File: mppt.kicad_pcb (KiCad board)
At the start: 2 copper layers, 52 parts, among them P101 CONN_01X02, P102 CONN_01X02, P103 JTAG, P104 CONN_01X02, Q201 IRF7343PBF, U102 STM32F103C8Tx, U104 SN65HVD12DR, U201 358, U202 358, U301 lm2575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

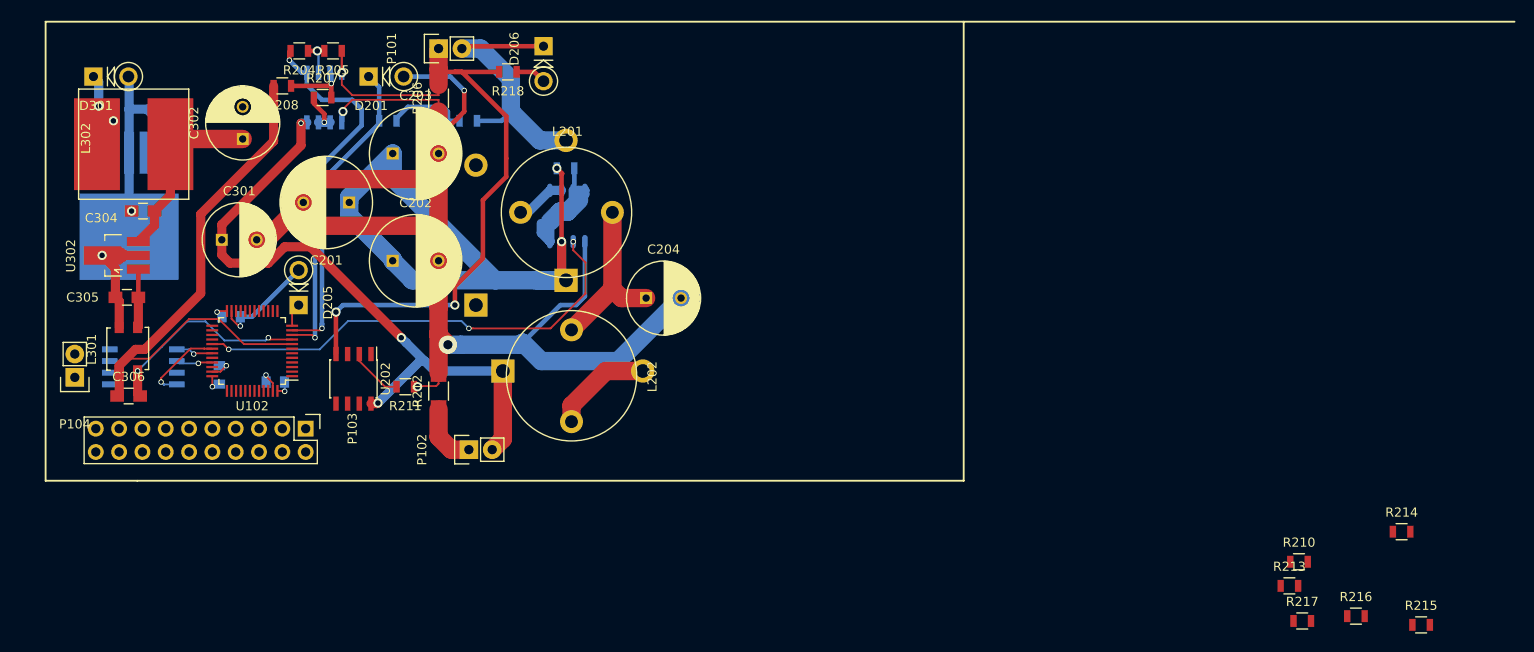
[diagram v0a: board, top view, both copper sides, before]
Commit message: Changed a bit, and did a full re-route
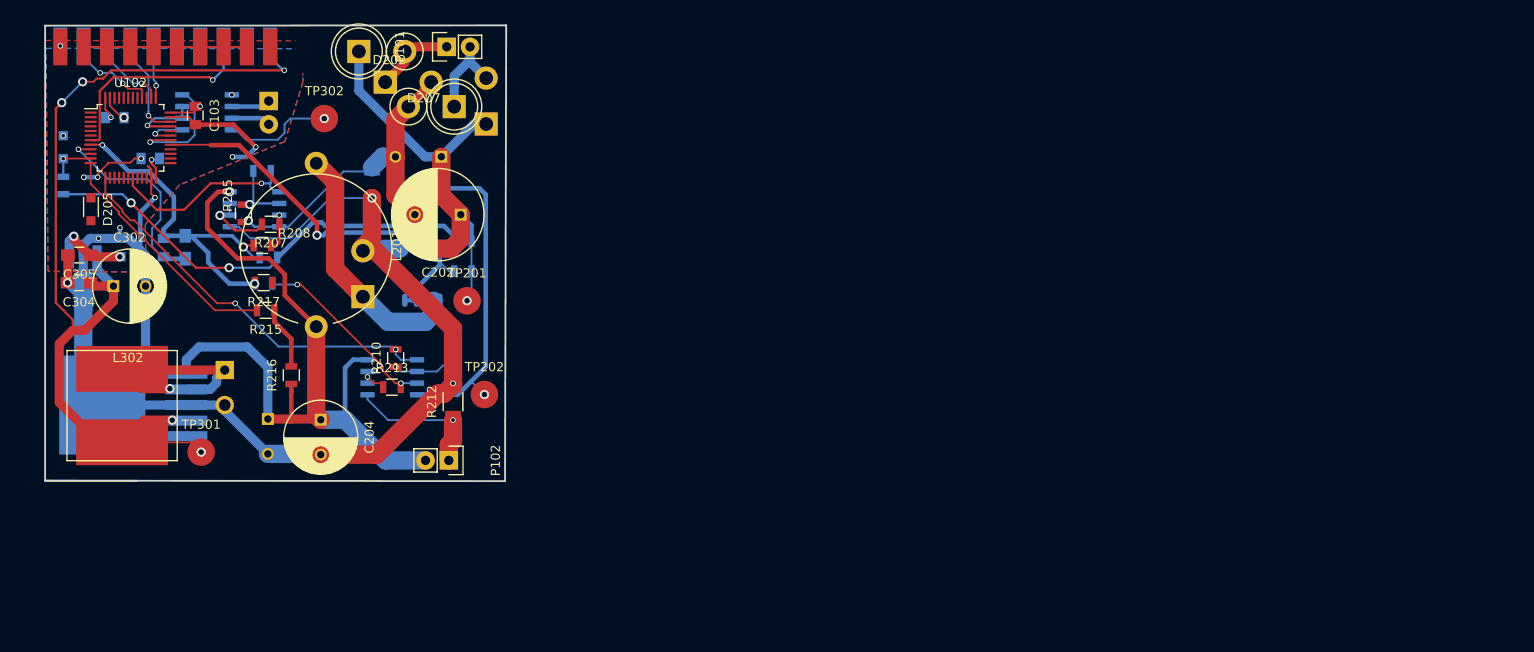
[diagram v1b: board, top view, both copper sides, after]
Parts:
- removed C203: CP, Capacitors_ThroughHole:C_Radial_D10_L16_P5
- removed L202: L, Inductors_NEOSID:Neosid_Inductor_Sd14
- removed R218: R, Resistors_SMD:R_0805
- removed U104: SN65HVD12DR, Housings_SOIC:SOIJ-8_5.3x5.3mm_Pitch1.27mm
- added D207: D_Schottky, lib:Diode_DO-201AD_Vertical, F.Cu at (74.1, 43.2)
- added TP201: TEST, Measurement_Points:Measurement_Point_Round-SMD-Pad_Big, F.Cu at (85.9, 70.4)
- added TP202: TEST, Measurement_Points:Measurement_Point_Round-SMD-Pad_Big, F.Cu at (87.8, 80.6)
- added TP301: TEST, Measurement_Points:Measurement_Point_Round-SMD-Pad_Big, F.Cu at (56.9, 86.9)
- added TP302: TEST, Measurement_Points:Measurement_Point_Round-SMD-Pad_Big, F.Cu at (70.4, 50.6)
- added U101: ST3485ECDR, Housings_SOIC:SOIC-8_3.9x4.9mm_Pitch1.27mm, B.Cu at (57.6, 49.9)
- C103: moved to F.Cu
- C201: value CP -> 100uF; moved to B.Cu
- C202: value CP -> 100uF
- C301, C306, D301, L301, P104, R204, R206, R211, R214, U202, U302: moved to B.Cu
- D201: footprint Diodes_ThroughHole:Diode_DO-41_SOD81_Vertical_KathodeUp -> Diodes_SMD:SOD-323_HandSoldering; moved to B.Cu
- D202: footprint Diodes_ThroughHole:Diode_DO-201AD_Horizontal_RM15 -> lib:Diode_DO-201AD_Vertical; moved to F.Cu
- D203, D204: footprint Diodes_ThroughHole:Diode_DO-201AD_Horizontal_RM15 -> lib:Diode_DO-201AD_Vertical
- D205: footprint Diodes_ThroughHole:Diode_DO-41_SOD81_Vertical_KathodeUp -> Diodes_SMD:SOD-323_HandSoldering
- D206: value D -> D_Schottky; footprint Diodes_ThroughHole:Diode_DO-41_SOD81_Vertical_KathodeUp -> lib:Diode_DO-201AD_Vertical; moved to B.Cu
- L201: footprint Inductors_NEOSID:Neosid_Inductor_Sd14 -> PCV-0-104-05L
- P103: footprint Pin_Headers:Pin_Header_Straight_2x10 -> lib:20p_edge; moved to B.Cu
- moved R215 130.4 mm to (64.0, 71.4), turned to 180 degrees
- moved R214 126.9 mm to (63.7, 68.5), turned to 180 degrees
- moved R217 119.0 mm to (63.8, 68.4), turned to 180 degrees
- moved R216 118.9 mm to (66.8, 78.5), turned to 90 degrees
- moved R210 100.9 mm to (78.1, 76.6), turned to 90 degrees
- moved R213 100.1 mm to (77.7, 79.8)
- moved P103 42.5 mm to (53.0, 44.6), turned to 0 degrees
- moved C204 37.8 mm to (70.0, 83.4), turned to 270 degrees
- moved P104 36.8 mm to (64.3, 48.6)
- moved R203 36.0 mm to (41.9, 57.8), turned to 90 degrees
- moved D301 35.0 mm to (59.5, 77.9), turned to 270 degrees
- moved D201 34.1 mm to (41.9, 53.7), turned to 90 degrees
- moved C102 33.7 mm to (47.5, 50.4), turned to 0 degrees
- moved L302 28.5 mm to (48.3, 81.8), turned to 0 degrees
- moved C103 28.4 mm to (56.3, 50.2), turned to 270 degrees
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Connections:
- C201 pad 1: Net-(C201-Pad1) -> /regulator/in_rect+
- C201 pad 2: GND -> /regulator/in_rect-
- C202 pad 1: Net-(C201-Pad1) -> /regulator/in_rect+
- C202 pad 2: GND -> /regulator/in_rect-
- C204 pad 1: Net-(C204-Pad1) -> +24V
- D202 pad 1: Net-(C201-Pad1) -> /regulator/GENERATOR_IN+
- D202 pad 2: /regulator/GENERATOR_IN+ -> /regulator/in_rect-
- D204 pad 1: +24V -> /regulator/in_rect+
- D204 pad 2: Net-(D204-Pad2) -> /regulator/GENERATOR_IN+
- D206 pad 1: /regulator/GENERATOR_IN+ -> /regulator/GENERATOR_IN-
- D206 pad 2: Net-(D206-Pad2) -> /regulator/in_rect-
- L201 pad 2: Net-(C204-Pad1) -> +24V
- Q201 pad 3: Net-(C201-Pad1) -> /regulator/in_rect+
- R201 pad 1: /regulator/GENERATOR_IN+ -> /regulator/in_rect+
- R204 pad 2: /regulator/Iin -> /Iin
- R205 pad 1: /regulator/GENERATOR_IN- -> /regulator/in_rect-
- R206 pad 2: /regulator/GENERATOR_IN- -> /regulator/in_rect-
- R209 pad 1: Net-(C201-Pad1) -> /regulator/in_rect+
- U102 pad 10: /regulator/Iin -> (no net)
- U102 pad 19: (no net) -> /Iin
- U201 pad 1: /regulator/Iin -> /Iin
- U201 pad 4: /regulator/GENERATOR_IN- -> /regulator/in_rect-
- U202 pad 4: /regulator/GENERATOR_IN- -> /regulator/in_rect-
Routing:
- net +5V: track 20.2 -> 101.5 mm, vias 0 -> 5
- net /regulator/in_rect-: track 0.00 -> 75.5 mm, vias 0 -> 2
- net Net-(C201-Pad1): track 74.1 -> 0.00 mm, vias 2 -> 0
- net /regulator/GENERATOR_IN-: track 75.5 -> 9.01 mm, vias 3 -> 0
- net /regulator/in_rect+: track 0.00 -> 49.5 mm, vias 0 -> 3
- net /regulator/Iout: track 0.00 -> 43.6 mm, vias 0 -> 2
- net /regulator/Iin: track 41.5 -> 0.00 mm, vias 2 -> 0
- net Net-(R201-Pad2): track 10.0 -> 49.2 mm, vias 0 -> 2
- net /regulator/Uin: track 34.1 -> 4.97 mm
- net /regulator/Ubat: track 2.55 -> 26.2 mm
- net GNDA: track 63.8 -> 40.2 mm, vias 0 -> 3
- net /nrst: track 0.00 -> 23.5 mm, vias 0 -> 1
- net Net-(D203-Pad1): track 5.46 -> 28.6 mm
- net /Iin: track 0.00 -> 21.1 mm, vias 0 -> 1
- net GND: track 202.0 -> 222.6 mm, vias 9 -> 14
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- added copper zone on B.Cu, net +3V3
- added copper zone on F.Cu, net GND
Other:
- board outline added: 50.2 x 49.6 mm

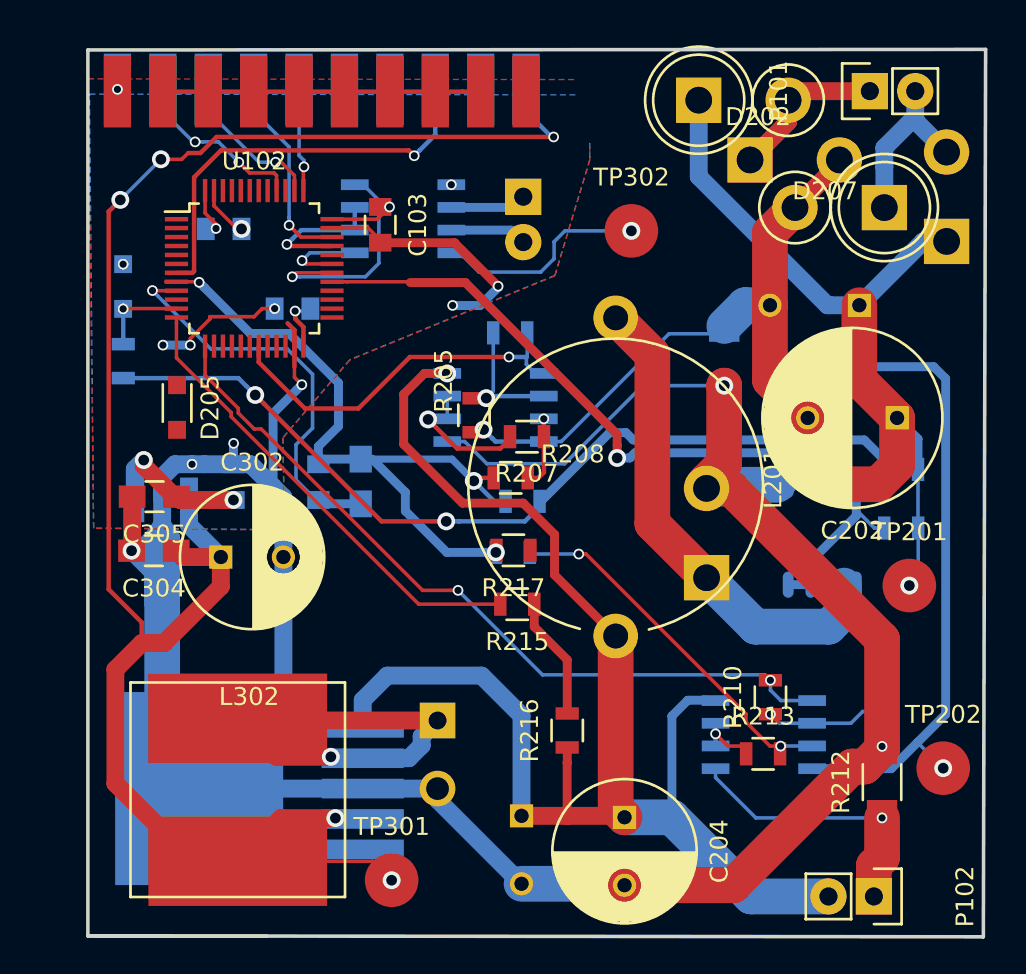
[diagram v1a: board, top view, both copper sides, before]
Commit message: Routed for 5x5 pcb
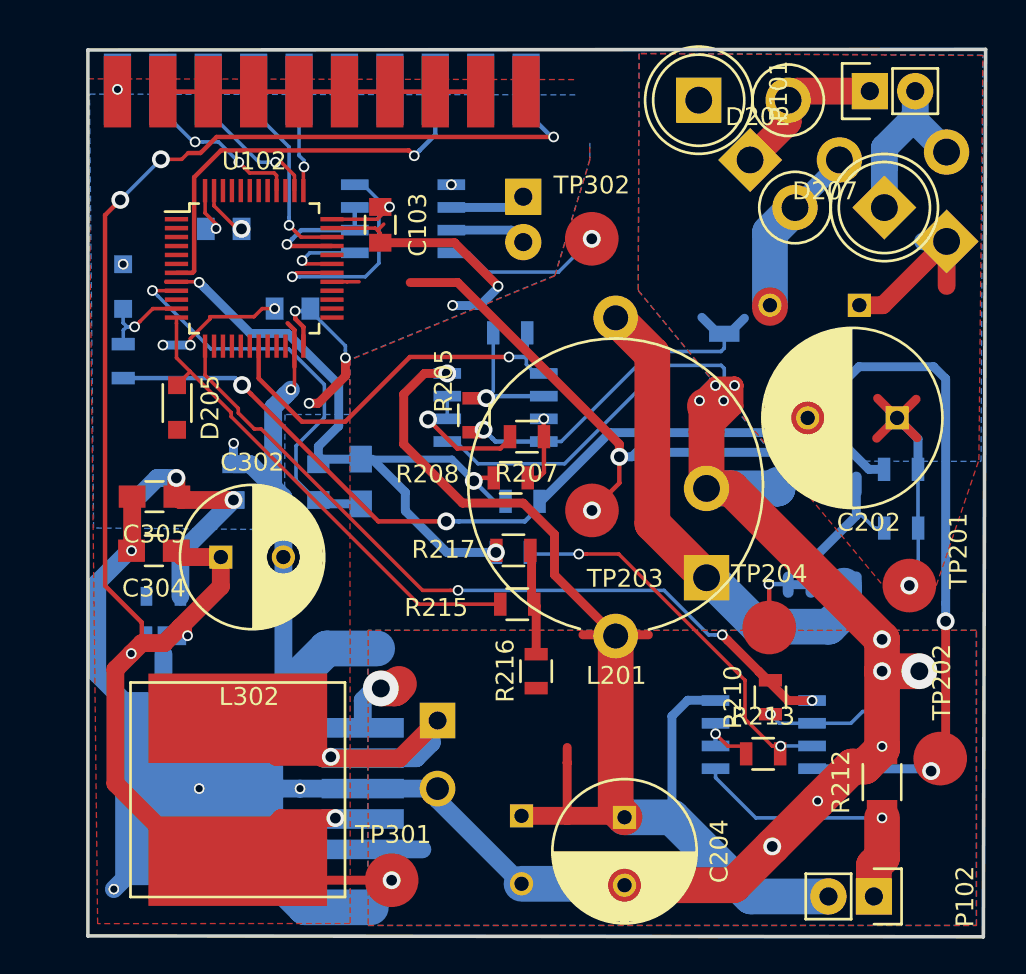
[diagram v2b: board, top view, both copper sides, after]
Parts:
- added TP203: TEST, Measurement_Points:Measurement_Point_Round-SMD-Pad_Big, F.Cu at (68.1, 66.2)
- added TP204: TEST, Measurement_Points:Measurement_Point_Round-SMD-Pad_Big, F.Cu at (78.1, 72.7)
- C305: value 1u -> 2u
- U302: value LM78L33 -> mic5205; footprint TO_SOT_Packages_SMD:SOT89-3_Housing_Handsoldering -> TO_SOT_Packages_SMD:SOT-23-5
- moved U302 4.15 mm to (44.2, 72.1), turned to 90 degrees
- moved R216 3.75 mm to (65.0, 75.2)
- moved TP302 2.26 mm to (68.1, 51.0)
- moved TP202 0.56 mm to (87.6, 80.1)
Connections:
- U302 pad 1: +3V3 -> +5V
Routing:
- net GND: track 222.6 -> 277.7 mm, vias 14 -> 24
- net /regulator/in_rect+: track 49.5 -> 29.1 mm, vias 3 -> 4
- net +3V3: track 30.2 -> 39.6 mm, vias 7 -> 9
- net +24V: track 82.6 -> 73.1 mm, vias 1 -> 2
- net Net-(Q201-Pad4): track 11.3 -> 14.8 mm, vias 0 -> 1
- net Net-(D301-Pad1): track 22.7 -> 24.7 mm
- net /regulator/in_rect-: track 75.5 -> 73.6 mm, vias 2 -> 3
- net +5V: track 101.5 -> 100.3 mm, vias 5 -> 7
- net /Iin: track 21.1 -> 22.3 mm
- net /regulator/Ubat: track 26.2 -> 27.3 mm
- net Net-(R213-Pad2): track 20.5 -> 21.5 mm
- net Net-(R215-Pad1): track 6.88 -> 5.94 mm
- net /regulator/Uin: track 4.97 -> 5.78 mm
- net Net-(R210-Pad1): track 7.37 -> 6.73 mm
- net VDDA: track 22.7 -> 23.3 mm
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- added copper zone on F.Cu, net +24V
- added copper zone on F.Cu, net /regulator/in_rect+
- added copper zone on B.Cu, net /regulator/in_rect-
- added copper zone on B.Cu, net GND
